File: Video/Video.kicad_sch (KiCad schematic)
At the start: 208 parts, among them J1 Conn_02x22_Top_Bottom, J2 Conn_02x22_Top_Bottom, J3 Conn_02x22_Top_Bottom, Q1 Q_NPN_BCE, U1 74LS07, U10 74LS32, U100 74LS161, U101 74LS20, U102 74LS161, U103 74LS161, U104 74LS32, U105 74LS153, U106 MB7137, U107 74LS161, U108 74LS161, U109 74LS107, U11 74LS157, U110 74LS00, U111 74LS157, U112 74LS153, U113 MB7137, U114 74LS06, U115 74LS10, U116 74LS107, U117 74LS06, U118 74LS161, U119 74LS153, U12 MB7137, U120 MB7137, U13 74LS30, U14 74LS20, U15 74LS09, U16 74LS00, U17 MB7137, U18 74LS123, U19 74LS12, U2 74LS147, U20 74LS157, U201 74LS393, U202 74LS157, U203 74LS157, U204 74LS86, U205 74LS157, U206 74LS74, U21 74LS11, U22 74LS06, U23 74LS86, U24 74LS42, U25 74LS74, U26 74LS20, U27 74LS30, U28 74LS86, U29 74LS157, U3 74LS04, U30 MB7137, U31 74LS74, U32 74LS21, U33 74LS30, U34 74LS02, U35 74LS74, U36 74LS161, U37 74LS161, U38 74LS74, U39 74LS32, U4 74LS30, U40 74LS74, U41 74LS151, U42 74LS10, U43 74LS157, U44 74LS10, U45 74LS00, U46 74LS193, U47 74LS08, U48 74LS151, U49 74LS393, U5 74LS157, U50 74LS157, U51 MB7137, U52 74LS08, U53 74LS153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

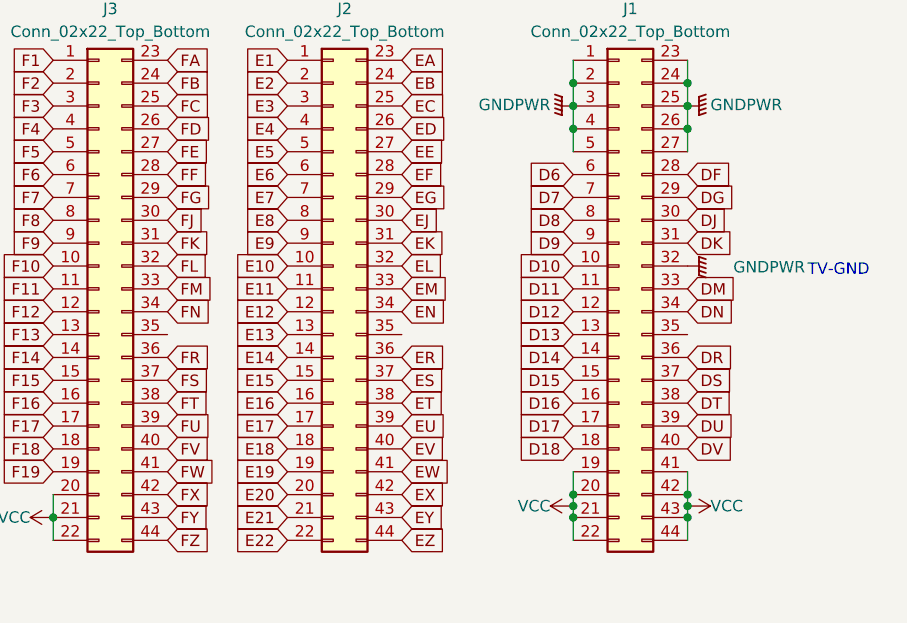
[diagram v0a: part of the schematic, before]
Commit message: fixed some warnings
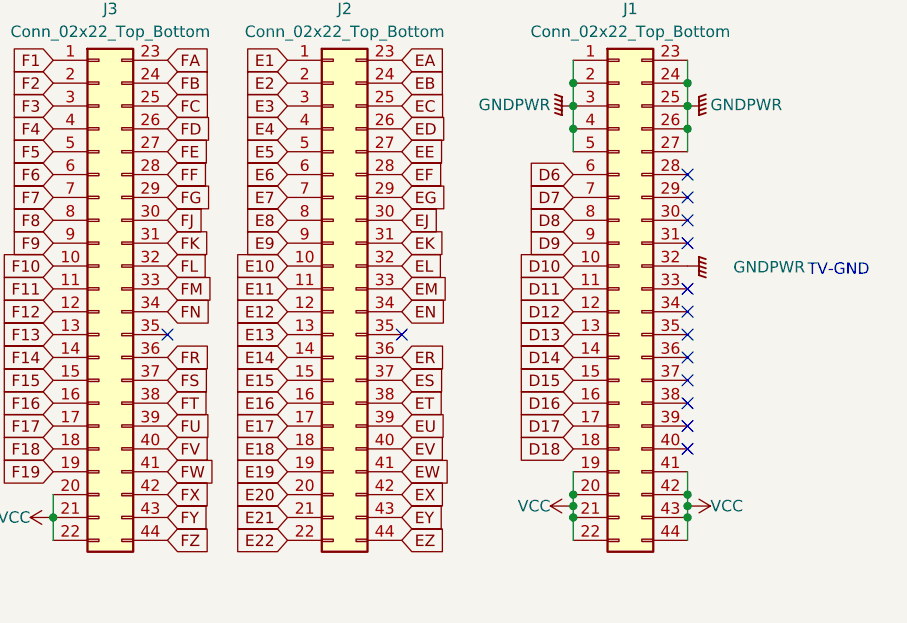
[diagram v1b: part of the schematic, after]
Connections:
- net DF: no longer names the net of J1.28 (Pin_28)
- net DG: no longer names the net of J1.29 (Pin_29)
- net DJ: no longer names the net of J1.30 (Pin_30)
- net DK: no longer names the net of J1.31 (Pin_31)
- net DM: no longer names the net of J1.33 (Pin_33)
- net DN: no longer names the net of J1.34 (Pin_34)
- net DR: no longer names the net of J1.36 (Pin_36)
- net DS: no longer names the net of J1.37 (Pin_37)
- net DT: no longer names the net of J1.38 (Pin_38)
- net DU: no longer names the net of J1.39 (Pin_39)
- net DV: no longer names the net of J1.40 (Pin_40)
- no-connect marks 141 -> 155

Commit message: rom names
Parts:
- removed J1, J2, J3: Conn_02x22_Top_Bottom, BoardEdge:EdgeD, symbol Connector_Generic:Conn_02x22_Top_Bottom
- U106: value MB7137 -> pra135.ic106
- U113: value MB7137 -> pra134.ic113
- U12: value MB7137 -> pra140.ic12
- U120: value MB7137 -> pra137.ic120
- U17: value MB7137 -> pra141.ic17
- U51: value MB7137 -> pra139.ic51
- U64: value MB7137 -> pra133.ic64
- U99: value MB7137 -> pra136.ic99

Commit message: convert
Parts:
- removed TP1: TestPoint, TestPoint:TestPoint_Loop_D2.60mm_Drill0.9mm_Beaded, symbol Connector:TestPoint
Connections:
- net 7MHz: no longer U117.6, U36.2 (CP), U37.2 (CP)
- net EF: no longer U31.8 (~{Q}), U34.4, U38.12 (D), U80.11, U95.9
- net FF: no longer U101.1, U109.3 (Q), U110.2, U114.1, U115.2, U53.1 (Ea), U55.4, U64.1 (A7)
- net GNDPWR: no longer U12.21 (A10), U51.21 (A10), U64.21 (A10)
- net at U11.5 (I0b), U17.10 (D1): no longer U12.10 (D1)
- net at U11.11 (I0c), U17.11 (D2): no longer U12.11 (D2)
- net at U11.14 (I0d), U17.13 (D3): no longer U12.13 (D3)
- net at U11.3 (I1a), U17.14 (D4): no longer U12.14 (D4)
- net at U11.6 (I1b), U17.15 (D5): no longer U12.15 (D5)
- net at U11.10 (I1c), U17.16 (D6): no longer U12.16 (D6)
- net at U11.13 (I1d), U17.17 (D7): no longer U12.17 (D7)
- net at U10.11, U12.18 (CE2), U12.19 (CE3)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: no longer U17.21 (A10)
- net at U11.2 (I0a), U17.9 (D0): no longer U12.9 (D0)
- net at U30.21 (A10): no longer U204.5
- new net: U101.1, U109.3 (Q), U110.2, U114.1, U115.2
- new net: U31.8 (~{Q}), U38.12 (D)
- new net F13: U117.6, U36.2 (CP), U37.2 (CP)
- new net H8: U53.1 (Ea), U55.4, U64.1 (A7)
- new net ~{TUNNEL&BRIDGE}: U34.4, U80.11, U95.9
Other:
- moved on the sheet: C13, C14, C16, C17, C19, C2, C8, C998, R17, R18, R2077, U100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

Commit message: drc
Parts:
- added J1, J2, J3: Conn_02x22_Top_Bottom, BoardEdge:EdgeD, symbol Connector_Generic:Conn_02x22_Top_Bottom
- added TP1: TestPoint, TestPoint:TestPoint_Loop_D2.60mm_Drill0.9mm_Beaded, symbol Connector:TestPoint
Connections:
- net FF is gone; now on net H8: U102.6 (D3), U115.10, U116.10 (~{R}), U116.11 (K), U116.3 (Q), U116.8 (J)
- net 14MHz: now also J2.40 (Pin_40)
- net 14MHz_EXT: now also J1.6 (Pin_6)
- net ACCE.D: now also J3.14 (Pin_14)
- net AREA 1: now also J2.32 (Pin_32)
- net AREA 2: now also J2.31 (Pin_31)
- net AREA 3: now also J2.9 (Pin_9)
- net AREA 4: now also J2.10 (Pin_10)
- net AREA 5: now also J2.11 (Pin_11)
- net BRIDGE AP: now also J2.18 (Pin_18)
- net COIN IN: now also J3.1 (Pin_1)
- net D14: now also J1.14 (Pin_14)
- net D15: now also J1.15 (Pin_15)
- net D16: now also J1.16 (Pin_16)
- net D17: now also J1.17 (Pin_17)
- net D18: now also J1.18 (Pin_18)
- net D7: now also J1.7 (Pin_7)
- net D8: now also J1.8 (Pin_8)
- net D9: now also J1.9 (Pin_9)
- net E12: now also J3.12 (Pin_12)
- net E18: now also J3.18 (Pin_18)
- net E19: now also J3.19 (Pin_19)
- net E2: now also J3.2 (Pin_2); no longer U72.4
- net E20: now also J3.20 (Pin_20)
- net E21: now also J3.21 (Pin_21)
- net E22: now also J3.22 (Pin_22)
- net E3: now also J3.3 (Pin_3)
- net EA: now also J3.23 (Pin_23)
- net EB: now also J3.24 (Pin_24)
- net ED: now also J3.26 (Pin_26)
- net EE: now also J3.27 (Pin_27)
- net EG: now also J3.29 (Pin_29)
- net EN: now also J3.34 (Pin_34)
- net EW: now also J3.41 (Pin_41)
- net EX: now also J3.42 (Pin_42)
- net EY: now also J3.43 (Pin_43)
- net EZ: now also J3.44 (Pin_44)
- net F12: now also J2.12 (Pin_12)
- net F14: now also J2.14 (Pin_14)
- net F16: now also J2.16 (Pin_16)
- net F17: now also J2.17 (Pin_17)
- net F19: now also J2.19 (Pin_19)
- net F2: now also J2.2 (Pin_2)
- net F4: now also J2.4 (Pin_4)
- net F5: now also J2.5 (Pin_5)
- net F7: now also J2.7 (Pin_7)
- net F8: now also J2.8 (Pin_8)
- net FA: now also J2.23 (Pin_23)
- net FB: now also J2.24 (Pin_24)
- net FC: now also J2.25 (Pin_25)
- net FD: now also J2.26 (Pin_26)
- net FE: now also J2.27 (Pin_27)
- net FG: now also J2.29 (Pin_29)
- net FJ: now also J2.30 (Pin_30)
- net FM: now also J2.33 (Pin_33)
- net FN: now also J2.34 (Pin_34)
- net FR: now also J2.36 (Pin_36)
- net FT: now also J2.38 (Pin_38)
- net FU: now also J2.39 (Pin_39)
- net GNDPWR: now also U12.21 (A10), U51.21 (A10), U64.21 (A10), J1.1 (Pin_1), J1.2 (Pin_2), J1.23 (Pin_23), J1.24 (Pin_24), J1.25 (Pin_25), J1.26 (Pin_26), J1.27 (Pin_27), J1.3 (Pin_3), J1.32 (Pin_32), J1.4 (Pin_4), J1.5 (Pin_5)
- net H8: now also U101.1, U109.3 (Q), U110.2, U114.1, U115.2, J2.28 (Pin_28)
- net V2: now also J2.6 (Pin_6)
- net VCC: now also J1.19 (Pin_19), J1.20 (Pin_20), J1.21 (Pin_21), J1.22 (Pin_22), J1.41 (Pin_41), J1.42 (Pin_42), J1.43 (Pin_43), J1.44 (Pin_44), J2.20 (Pin_20), J2.21 (Pin_21), J2.22 (Pin_22), J2.42 (Pin_42), J2.43 (Pin_43), J2.44 (Pin_44)
- net ~{TUNNEL&BRIDGE}: now also U31.8 (~{Q}), U38.12 (D), J3.28 (Pin_28)
- net BRIDGE_ROM_D1: now reaches U11.5 (I0b), U17.10 (D1)
- net BRIDGE_ROM_D1: now also U12.10 (D1)
- net BRIDGE_ROM_D2: now reaches U11.11 (I0c), U17.11 (D2)
- net BRIDGE_ROM_D2: now also U12.11 (D2)
- net BRIDGE_ROM_D3: now reaches U11.14 (I0d), U17.13 (D3)
- net BRIDGE_ROM_D3: now also U12.13 (D3)
- net BRIDGE_ROM_D4: now reaches U11.3 (I1a), U17.14 (D4)
- net BRIDGE_ROM_D4: now also U12.14 (D4)
- net BRIDGE_ROM_D5: now reaches U11.6 (I1b), U17.15 (D5)
- net BRIDGE_ROM_D5: now also U12.15 (D5)
- net BRIDGE_ROM_D6: now reaches U11.10 (I1c), U17.16 (D6)
- net BRIDGE_ROM_D6: now also U12.16 (D6)
- net BRIDGE_ROM_D7: now reaches U11.13 (I1d), U17.17 (D7)
- net BRIDGE_ROM_D7: now also U12.17 (D7)
- net at U10.11, U12.18 (CE2), U12.19 (CE3)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: now also U17.21 (A10)
- net BRIDGE_ROM_D0: now reaches U11.2 (I0a), U17.9 (D0)
- net BRIDGE_ROM_D0: now also U12.9 (D0)
- net at U30.21 (A10): now also U204.5
- net at U33.4: now also TP1.1
- net D10 renamed TV-SYNC
- net TV-SYNC: now also J1.10 (Pin_10)
- net D11 renamed TV-RED
- net TV-RED: now also J1.11 (Pin_11)
- net D12 renamed TV-BLUE
- net TV-BLUE: now also J1.12 (Pin_12)
- net D13 renamed TV-GREEN
- net TV-GREEN: now also J1.13 (Pin_13)
- net E10 renamed ~{SPLAY}
- net ~{SPLAY}: now also J3.10 (Pin_10)
- net E15 renamed ~{OTHER CAR}
- net ~{OTHER CAR}: now also J3.15 (Pin_15)
- net E16 renamed GAME OVER
- net GAME OVER: now also J3.16 (Pin_16)
- net E17 renamed ~{PLAYER TIRE}
- net ~{PLAYER TIRE}: now also J3.17 (Pin_17)
- net E4 renamed ~{EXPLO.}
- net ~{EXPLO.}: now also J3.4 (Pin_4)
- net E6 renamed ~{GAME}
- net ~{GAME}: now also J3.6 (Pin_6)
- net E7 renamed ROAD
- net ROAD: now also J3.7 (Pin_7)
- net E8 renamed ~{RESCUE (Y)}
- net ~{RESCUE (Y)}: now also J3.8 (Pin_8)
- net E9 renamed ~{PLAYER}
- net ~{PLAYER}: now also J3.9 (Pin_9)
- net EC renamed ~{LIGHT}
- net ~{LIGHT}: now also J3.25 (Pin_25)
- net EJ renamed ~{EXT.500}
- net ~{EXT.500}: now also J3.30 (Pin_30)
- net EK renamed ~{EXPLO (R)}
- net ~{EXPLO (R)}: now also J3.31 (Pin_31)
- net EM renamed EXPLO SEL
- net EXPLO SEL: now also J3.33 (Pin_33)
- net ER renamed ~{OTHER BODY}
- net ~{OTHER BODY}: now also J3.36 (Pin_36)
- net ES renamed ~{OTHER TIRE}
- net ~{OTHER TIRE}: now also J3.37 (Pin_37)
- net ET renamed PLAYER BODY
- net PLAYER BODY: now also J3.38 (Pin_38)
- net EU renamed ~{PLAYER (BL)}
- net ~{PLAYER (BL)}: now also J3.39 (Pin_39)
- net EV renamed Vs/64
- net Vs/64: now also J3.40 (Pin_40)
- net F13 renamed ~{7MHz}
- net ~{7MHz}: now also J2.13 (Pin_13)
- net F15 renamed ~{EXPLO. AREA}
- net ~{EXPLO. AREA}: now also J2.15 (Pin_15)
- net F3 renamed ~{CAR NO CONT}
- net ~{CAR NO CONT}: now also J2.3 (Pin_3)
- net FS renamed ~{V-CAXVb}
- net ~{V-CAXVb}: now also J2.37 (Pin_37)
- new net EX.SIGNAL: J2.1 (Pin_1), U72.4
- no-connect marks 155 -> 160
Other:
- moved on the sheet: C1, Cp1, Cp10, Cp11, Cp12, Cp13, Cp14, Cp15, Cp16, Cp17, Cp18, Cp19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
